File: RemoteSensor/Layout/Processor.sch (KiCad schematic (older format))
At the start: 21 parts, among them J3 LCD_HEADER, Q3 2N7002, SW2 FLASH, U7 ESP-12F, U8 ds7505s+, U9 MCP23008-E_P

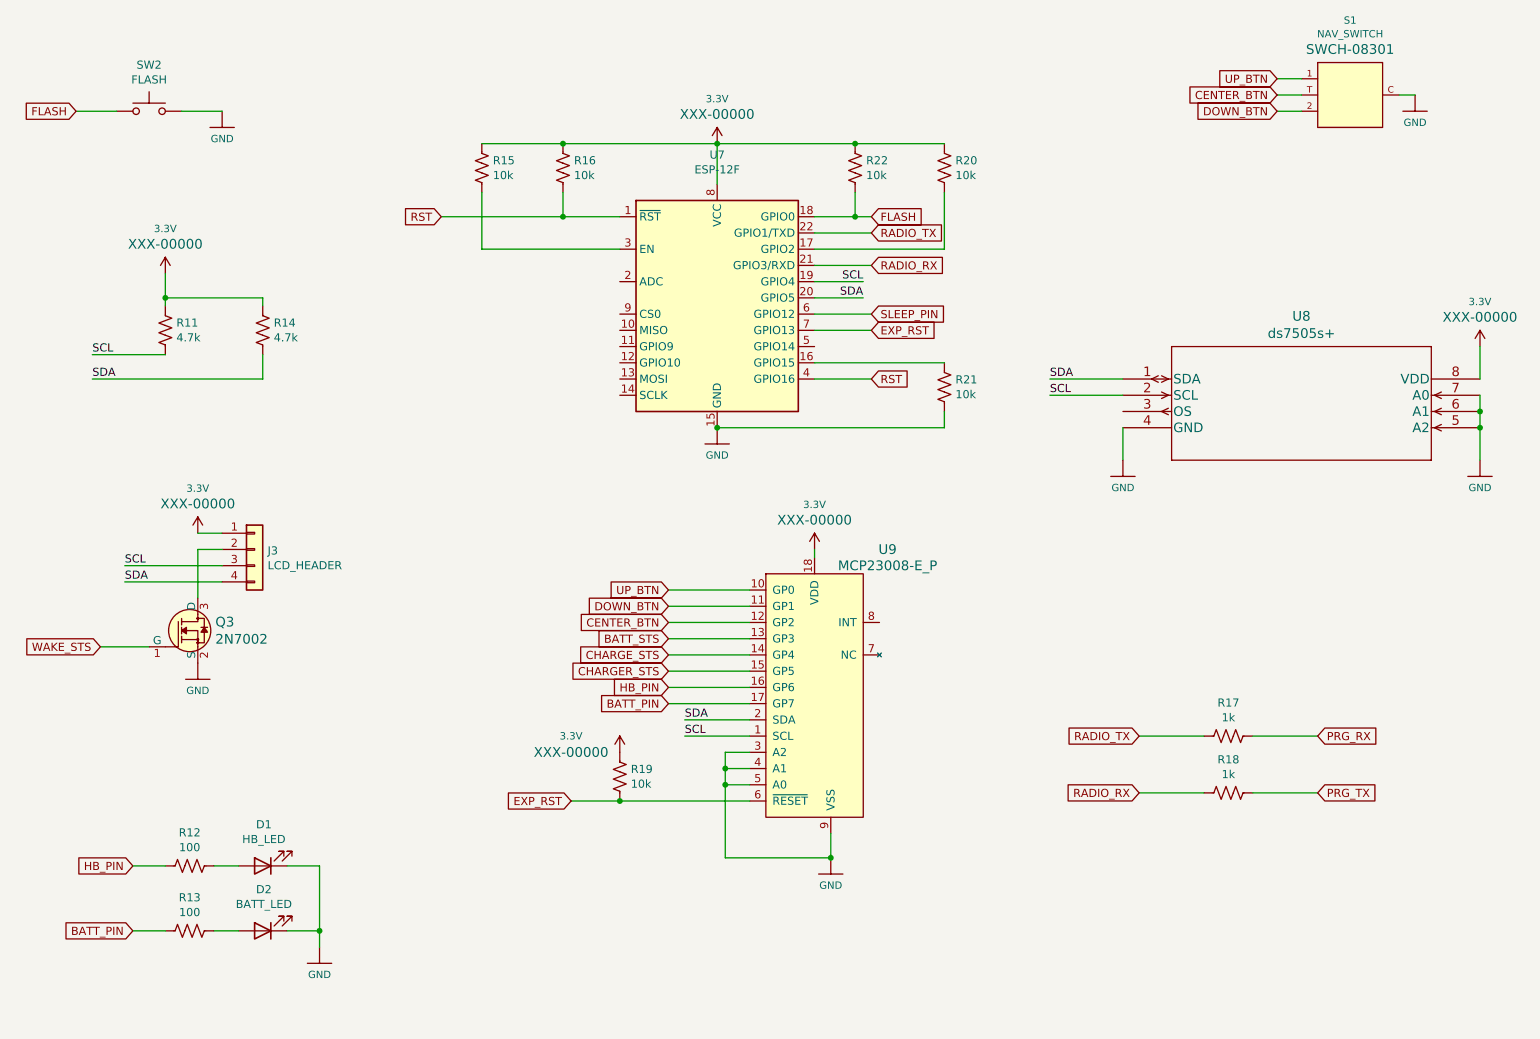
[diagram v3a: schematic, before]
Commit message: Change out nav switch for tactile
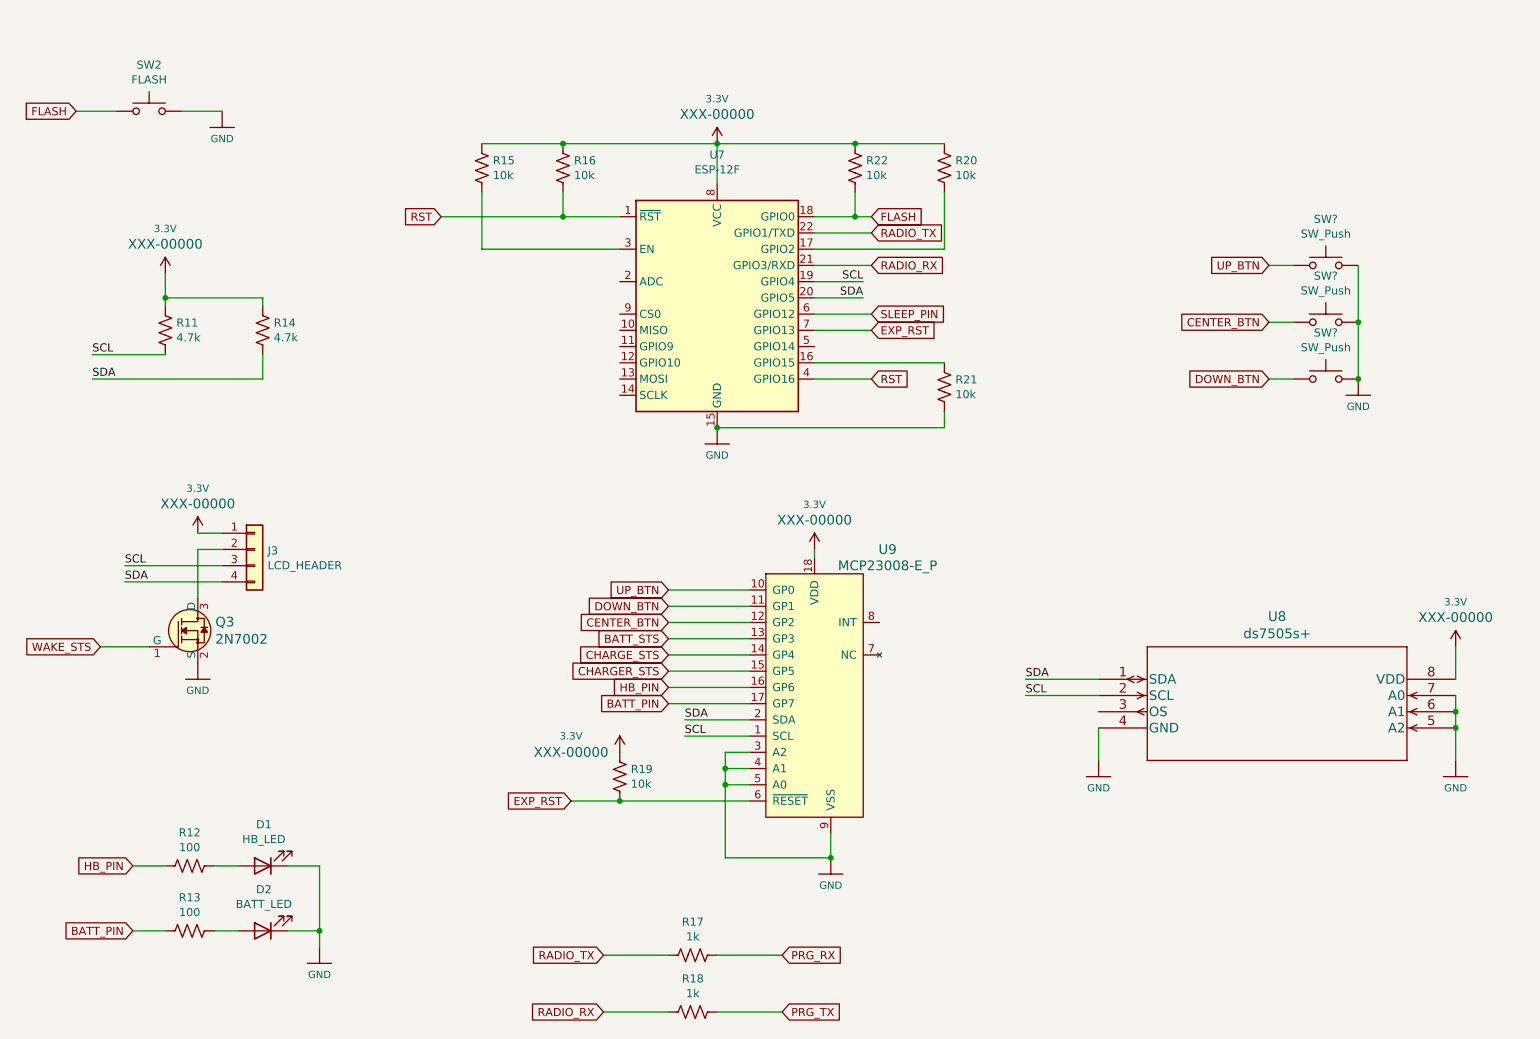
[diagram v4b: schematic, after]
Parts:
- removed S1: NAV_SWITCH, NAV_SWITCH, symbol RemoteSensor-rescue:NAV_SWITCH-SparkFun-Switches
- added SW? (x3): SW_Push, Button_Switch_THT:SW_Tactile_SPST_Angled_PTS645Vx58-2LFS, symbol Switch:SW_Push
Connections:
- net CENTER_BTN: now also SW?.1
- net DOWN_BTN: now also SW?.1
- net GND: now also SW?.2, SW?.2, SW?.2
- net UP_BTN: now also SW?.1
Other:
- moved on the sheet: R17, R18, U8
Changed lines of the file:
@@
-$EndComp
-$Comp
-L RemoteSensor-rescue:NAV_SWITCH-SparkFun-Switches S?
-U 1 1 5EF6B1EF
-P 9500 1200
-AR Path="/5EF6B1EF" Ref="S?"  Part="1"
-AR Path="/5EF5F91F/5EF6B1EF" Ref="S1"  Part="1"
-F 0 "S1" H 9500 1660 45  0000 C CNN
-F 1 "NAV_SWITCH" H 9500 1576 45  0000 C CNN
-F 2 "NAV_SWITCH" H 9500 1550 20  0001 C CNN
-F 3 "" H 9500 1200 50  0001 C CNN
-F 4 "SWCH-08301" H 9500 1481 60  0000 C CNN "Field4"
-	1    9500 1200
-	1    0    0    -1
 $EndComp
 $Comp
 L RemoteSensor-rescue:GND-SparkFun-PowerSymbols #GND?
 U 1 1 5EF6B1F5
-P 9900 1200
+P 9550 2950
 AR Path="/5EF6B1F5" Ref="#GND?"  Part="1"
 AR Path="/5EF5F91F/5EF6B1F5" Ref="#GND0115"  Part="1"
-F 0 "#GND0115" H 9950 1150 45  0001 L BNN
-F 1 "GND" H 9900 1030 45  0000 C CNN
-F 2 "" H 9900 1100 60  0001 C CNN
-F 3 "" H 9900 1100 60  0001 C CNN
-	1    9900 1200
-	1    0    0    -1
-$EndComp
-Wire Wire Line
-	9800 1200 9900 1200
+F 0 "#GND0115" H 9600 2900 45  0001 L BNN
+F 1 "GND" H 9550 2780 45  0000 C CNN
+F 2 "" H 9550 2850 60  0001 C CNN
+F 3 "" H 9550 2850 60  0001 C CNN
+	1    9550 2950
+	1    0    0    -1
+$EndComp
 $Comp
 L RemoteSensor-rescue:R_US-Device R?
 U 1 1 5EF7CD26
-P 8750 5150
+P 5450 6500
 AR Path="/5EF7CD26" Ref="R?"  Part="1"
 AR Path="/5EF5F91F/5EF7CD26" Ref="R17"  Part="1"
-F 0 "R17" V 8545 5150 50  0000 C CNN
-F 1 "1k" V 8636 5150 50  0000 C CNN
-F 2 "Resistor_SMD:R_0603_1608Metric_Pad1.05x0.95mm_HandSolder" V 8790 5140 50  0001 C CNN
-F 3 "~" H 8750 5150 50  0001 C CNN
-	1    8750 5150
+F 0 "R17" V 5245 6500 50  0000 C CNN
+F 1 "1k" V 5336 6500 50  0000 C CNN
+F 2 "Resistor_SMD:R_0603_1608Metric_Pad1.05x0.95mm_HandSolder" V 5490 6490 50  0001 C CNN
+F 3 "~" H 5450 6500 50  0001 C CNN
+	1    5450 6500
 	0    1    1    0
 $EndComp
@@
 L RemoteSensor-rescue:R_US-Device R?
 U 1 1 5EF7CD2C
-P 8750 5500
+P 5450 6850
 AR Path="/5EF7CD2C" Ref="R?"  Part="1"
 AR Path="/5EF5F91F/5EF7CD2C" Ref="R18"  Part="1"
-F 0 "R18" V 8545 5500 50  0000 C CNN
-F 1 "1k" V 8636 5500 50  0000 C CNN
-F 2 "Resistor_SMD:R_0603_1608Metric_Pad1.05x0.95mm_HandSolder" V 8790 5490 50  0001 C CNN
-F 3 "~" H 8750 5500 50  0001 C CNN
-	1    8750 5500
+F 0 "R18" V 5245 6850 50  0000 C CNN
+F 1 "1k" V 5336 6850 50  0000 C CNN
+F 2 "Resistor_SMD:R_0603_1608Metric_Pad1.05x0.95mm_HandSolder" V 5490 6840 50  0001 C CNN
+F 3 "~" H 5450 6850 50  0001 C CNN
+	1    5450 6850
 	0    1    1    0
 $EndComp
-Text GLabel 9050 1200 0    50   Input ~ 0
+Text GLabel 9000 2600 0    50   Input ~ 0
 CENTER_BTN
-Wire Wire Line
-	9050 1200 9200 1200
 Wire Wire Line
 	3900 1950 4650 1950
@@
 Text GLabel 6550 2050 2    50   Input ~ 0
 RADIO_TX
-Text GLabel 9050 1100 0    50   Input ~ 0
+Text GLabel 9000 2250 0    50   Input ~ 0
 UP_BTN
-Wire Wire Line
-	9050 1100 9200 1100
-Wire Wire Line
-	9050 1300 9200 1300
-Text GLabel 8200 5150 0    50   Input ~ 0
+Text GLabel 4900 6500 0    50   Input ~ 0
 RADIO_TX
-Text GLabel 8200 5500 0    50   Input ~ 0
+Text GLabel 4900 6850 0    50   Input ~ 0
 RADIO_RX
 Wire Wire Line
-	8200 5500 8600 5500
-Wire Wire Line
-	8200 5150 8600 5150
+	4900 6850 5300 6850
+Wire Wire Line
+	4900 6500 5300 6500
 Wire Wire Line
 	6200 2050 6550 2050
@@
 Text GLabel 6550 1950 2    50   Input ~ 0
 FLASH
-Text GLabel 9300 5150 2    50   Input ~ 0
+Text GLabel 6000 6500 2    50   Input ~ 0
 PRG_RX
-Text GLabel 9300 5500 2    50   Input ~ 0
+Text GLabel 6000 6850 2    50   Input ~ 0
 PRG_TX
 Wire Wire Line
-	8900 5150 9300 5150
-Wire Wire Line
-	8900 5500 9300 5500
+	5600 6500 6000 6500
+Wire Wire Line
+	5600 6850 6000 6850
 Text GLabel 5300 4350 0    50   Input ~ 0
 DOWN_BTN
 Text GLabel 5300 4250 0    50   Input ~ 0
 UP_BTN
-Text GLabel 9050 1300 0    50   Input ~ 0
+Text GLabel 9000 2950 0    50   Input ~ 0
 DOWN_BTN
 $Comp
@@
 L ds7505s:ds7505s+ U8
 U 1 1 5F5D9C9D
-P 8100 2950
-F 0 "U8" H 9200 3337 60  0000 C CNN
-F 1 "ds7505s+" H 9200 3231 60  0000 C CNN
-F 2 "Package_SO:SOIC-8_3.9x4.9mm_P1.27mm" H 9200 3190 60  0001 C CNN
-F 3 "" H 8100 2950 60  0000 C CNN
-	1    8100 2950
+P 7950 4800
+F 0 "U8" H 9050 5187 60  0000 C CNN
+F 1 "ds7505s+" H 9050 5081 60  0000 C CNN
+F 2 "Package_SO:SOIC-8_3.9x4.9mm_P1.27mm" H 9050 5040 60  0001 C CNN
+F 3 "" H 7950 4800 60  0000 C CNN
+	1    7950 4800
 	1    0    0    -1
 $EndComp
@@
 L SparkFun-PowerSymbols:3.3V #SUPPLY0119
 U 1 1 5F5DA98D
-P 10300 2750
-F 0 "#SUPPLY0119" H 10350 2750 45  0001 L BNN
-F 1 "3.3V" H 10300 3026 45  0000 C CNN
-F 2 "XXX-00000" H 10300 2931 60  0000 C CNN
-F 3 "" H 10300 2750 60  0001 C CNN
-	1    10300 2750
+P 10150 4600
+F 0 "#SUPPLY0119" H 10200 4600 45  0001 L BNN
+F 1 "3.3V" H 10150 4876 45  0000 C CNN
+F 2 "XXX-00000" H 10150 4781 60  0000 C CNN
+F 3 "" H 10150 4600 60  0001 C CNN
+	1    10150 4600
 	1    0    0    -1
 $EndComp
@@
 L SparkFun-PowerSymbols:GND #GND0117
 U 1 1 5F5DB10E
-P 8100 3450
-F 0 "#GND0117" H 8150 3400 45  0001 L BNN
-F 1 "GND" H 8100 3280 45  0000 C CNN
-F 2 "" H 8100 3350 60  0001 C CNN
-F 3 "" H 8100 3350 60  0001 C CNN
-	1    8100 3450
-	1    0    0    -1
-$EndComp
-Wire Wire Line
-	8100 3450 8100 3250
-Wire Wire Line
-	10300 2750 10300 2950
-Wire Wire Line
-	10300 3050 10300 3150
-Wire Wire Line
-	10300 3150 10300 3250
-Connection ~ 10300 3150
+P 7950 5300
+F 0 "#GND0117" H 8000 5250 45  0001 L BNN
+F 1 "GND" H 7950 5130 45  0000 C CNN
+F 2 "" H 7950 5200 60  0001 C CNN
+F 3 "" H 7950 5200 60  0001 C CNN
+	1    7950 5300
+	1    0    0    -1
+$EndComp
+Wire Wire Line
+	7950 5300 7950 5100
+Wire Wire Line
+	10150 4600 10150 4800
+Wire Wire Line
+	10150 4900 10150 5000
+Wire Wire Line
+	10150 5000 10150 5100
+Connection ~ 10150 5000
 $Comp
 L SparkFun-PowerSymbols:GND #GND0120
 U 1 1 5F5E5DFF
-P 10300 3450
-F 0 "#GND0120" H 10350 3400 45  0001 L BNN
-F 1 "GND" H 10300 3280 45  0000 C CNN
-F 2 "" H 10300 3350 60  0001 C CNN
-F 3 "" H 10300 3350 60  0001 C CNN
-	1    10300 3450
-	1    0    0    -1
-$EndComp
-Wire Wire Line
-	10300 3450 10300 3250
-Connection ~ 10300 3250
-Wire Wire Line
-	8100 2950 7650 2950
-Wire Wire Line
-	8100 3050 7650 3050
-Text Label 7650 2950 0    50   ~ 0
+P 10150 5300
+F 0 "#GND0120" H 10200 5250 45  0001 L BNN
+F 1 "GND" H 10150 5130 45  0000 C CNN
+F 2 "" H 10150 5200 60  0001 C CNN
+F 3 "" H 10150 5200 60  0001 C CNN
+	1    10150 5300
+	1    0    0    -1
+$EndComp
+Wire Wire Line
+	10150 5300 10150 5100
+Connection ~ 10150 5100
+Wire Wire Line
+	7950 4800 7500 4800
+Wire Wire Line
+	7950 4900 7500 4900
+Text Label 7500 4800 0    50   ~ 0
 SDA
-Text Label 7650 3050 0    50   ~ 0
+Text Label 7500 4900 0    50   ~ 0
 SCL
+$Comp
+L Switch:SW_Push SW?
+U 1 1 5F6BF1F9
+P 9350 2250
+F 0 "SW?" H 9350 2535 50  0000 C CNN
+F 1 "SW_Push" H 9350 2444 50  0000 C CNN
+F 2 "Button_Switch_THT:SW_Tactile_SPST_Angled_PTS645Vx58-2LFS" H 9350 2450 50  0001 C CNN
+F 3 "~" H 9350 2450 50  0001 C CNN
+	1    9350 2250
+	1    0    0    -1
+$EndComp
+$Comp
+L Switch:SW_Push SW?
+U 1 1 5F6C0B9B
+P 9350 2600
+F 0 "SW?" H 9350 2885 50  0000 C CNN
+F 1 "SW_Push" H 9350 2794 50  0000 C CNN
+F 2 "Button_Switch_THT:SW_Tactile_SPST_Angled_PTS645Vx58-2LFS" H 9350 2800 50  0001 C CNN
+F 3 "~" H 9350 2800 50  0001 C CNN
+	1    9350 2600
+	1    0    0    -1
+$EndComp
+$Comp
+L Switch:SW_Push SW?
+U 1 1 5F6C0F28
+P 9350 2950
+F 0 "SW?" H 9350 3235 50  0000 C CNN
+F 1 "SW_Push" H 9350 3144 50  0000 C CNN
+F 2 "Button_Switch_THT:SW_Tactile_SPST_Angled_PTS645Vx58-2LFS" H 9350 3150 50  0001 C CNN
+F 3 "~" H 9350 3150 50  0001 C CNN
+	1    9350 2950
+	1    0    0    -1
+$EndComp
+Wire Wire Line
+	9550 2250 9550 2600
+Connection ~ 9550 2600
+Wire Wire Line
+	9550 2600 9550 2950
+Connection ~ 9550 2950
+Wire Wire Line
+	9000 2950 9150 2950
+Wire Wire Line
+	9000 2600 9150 2600
+Wire Wire Line
+	9000 2250 9150 2250
 $EndSCHEMATC

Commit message: Another layout
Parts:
- J3: footprint Connector_PinHeader_2.54mm:PinHeader_1x04_P2.54mm_Vertical -> Connector_PinSocket_2.54mm:PinSocket_1x04_P2.54mm_Vertical
- SW3, SW4, SW5: renamed from SW?; footprint Button_Switch_THT:SW_Tactile_SPST_Angled_PTS645Vx58-2LFS -> Button_Switch_SMD:KSS331GLFS
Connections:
- net CENTER_BTN: now also U9.11 (GP1); no longer U9.12 (GP2)
- net DOWN_BTN: now also U9.10 (GP0); no longer U9.11 (GP1)
- net UP_BTN: now also U9.12 (GP2); no longer U9.10 (GP0)
- net EXP_INT: now reaches U9.8 (INT)
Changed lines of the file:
@@
 $EndComp
 Connection ~ 6300 5900
-Text GLabel 5300 4450 0    50   Input ~ 0
+Text GLabel 5300 4350 0    50   Input ~ 0
 CENTER_BTN
 Text Label 5400 5050 0    50   ~ 0
@@
 	7000 3250 5600 3250
 Connection ~ 5600 3250
-Wire Wire Line
-	5300 4250 5800 4250
-Wire Wire Line
-	5300 4350 5800 4350
-Wire Wire Line
-	5300 4450 5800 4450
 Text GLabel 5300 4550 0    50   Input ~ 0
 BATT_STS
@@
 Wire Wire Line
 	5600 6850 6000 6850
-Text GLabel 5300 4350 0    50   Input ~ 0
+Text GLabel 5300 4250 0    50   Input ~ 0
 DOWN_BTN
-Text GLabel 5300 4250 0    50   Input ~ 0
+Text GLabel 5300 4450 0    50   Input ~ 0
 UP_BTN
 Text GLabel 9000 2950 0    50   Input ~ 0
@@
 F 0 "J3" H 2830 3992 50  0000 L CNN
 F 1 "LCD_HEADER" H 2830 3901 50  0000 L CNN
-F 2 "Connector_PinHeader_2.54mm:PinHeader_1x04_P2.54mm_Vertical" H 2750 4000 50  0001 C CNN
+F 2 "Connector_PinSocket_2.54mm:PinSocket_1x04_P2.54mm_Vertical" H 2750 4000 50  0001 C CNN
 F 3 "~" H 2750 4000 50  0001 C CNN
 	1    2750 4000
@@
 SCL
 $Comp
-L Switch:SW_Push SW?
+L Switch:SW_Push SW3
 U 1 1 5F6BF1F9
 P 9350 2250
-F 0 "SW?" H 9350 2535 50  0000 C CNN
+F 0 "SW3" H 9350 2535 50  0000 C CNN
 F 1 "SW_Push" H 9350 2444 50  0000 C CNN
-F 2 "Button_Switch_THT:SW_Tactile_SPST_Angled_PTS645Vx58-2LFS" H 9350 2450 50  0001 C CNN
+F 2 "Button_Switch_SMD:KSS331GLFS" H 9350 2450 50  0001 C CNN
 F 3 "~" H 9350 2450 50  0001 C CNN
 	1    9350 2250
@@
 $EndComp
 $Comp
-L Switch:SW_Push SW?
+L Switch:SW_Push SW4
 U 1 1 5F6C0B9B
 P 9350 2600
-F 0 "SW?" H 9350 2885 50  0000 C CNN
+F 0 "SW4" H 9350 2885 50  0000 C CNN
 F 1 "SW_Push" H 9350 2794 50  0000 C CNN
-F 2 "Button_Switch_THT:SW_Tactile_SPST_Angled_PTS645Vx58-2LFS" H 9350 2800 50  0001 C CNN
+F 2 "Button_Switch_SMD:KSS331GLFS" H 9350 2800 50  0001 C CNN
 F 3 "~" H 9350 2800 50  0001 C CNN
 	1    9350 2600
@@
 $EndComp
 $Comp
-L Switch:SW_Push SW?
+L Switch:SW_Push SW5
 U 1 1 5F6C0F28
 P 9350 2950
-F 0 "SW?" H 9350 3235 50  0000 C CNN
+F 0 "SW5" H 9350 3235 50  0000 C CNN
 F 1 "SW_Push" H 9350 3144 50  0000 C CNN
-F 2 "Button_Switch_THT:SW_Tactile_SPST_Angled_PTS645Vx58-2LFS" H 9350 3150 50  0001 C CNN
+F 2 "Button_Switch_SMD:KSS331GLFS" H 9350 3150 50  0001 C CNN
 F 3 "~" H 9350 3150 50  0001 C CNN
 	1    9350 2950
@@
 Wire Wire Line
 	9000 2250 9150 2250
+Wire Wire Line
+	6600 4450 6900 4450
+Text GLabel 6900 4450 2    50   Input ~ 0
+EXP_INT
+Wire Wire Line
+	5300 4350 5800 4350
+Wire Wire Line
+	5300 4250 5800 4250
+Wire Wire Line
+	5800 4450 5300 4450
 $EndSCHEMATC
